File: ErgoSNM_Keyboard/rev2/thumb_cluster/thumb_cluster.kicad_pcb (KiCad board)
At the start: 2 copper layers, 57 x 38.2 mm, 19 parts, among them J1 Conn_01x08

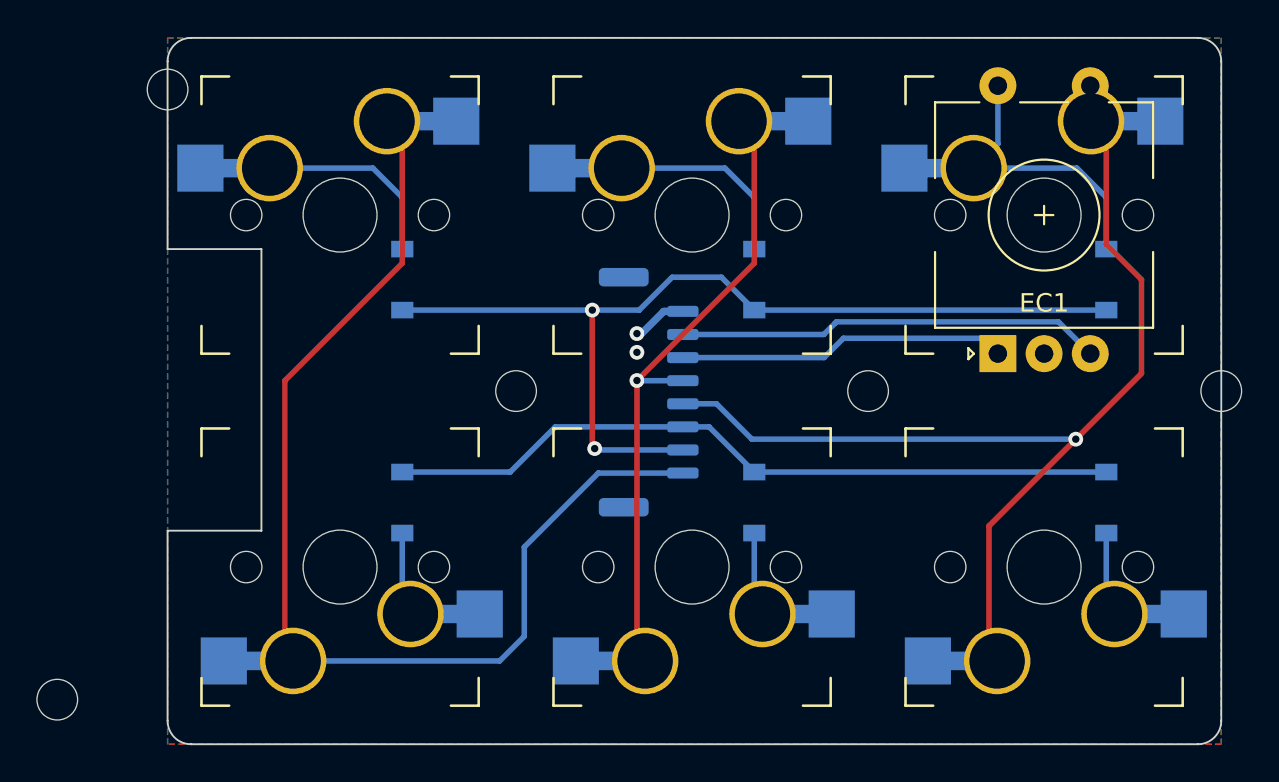
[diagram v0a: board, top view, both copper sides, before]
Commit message: Replace JST GH 1.25 connector with 0.5mm FPC
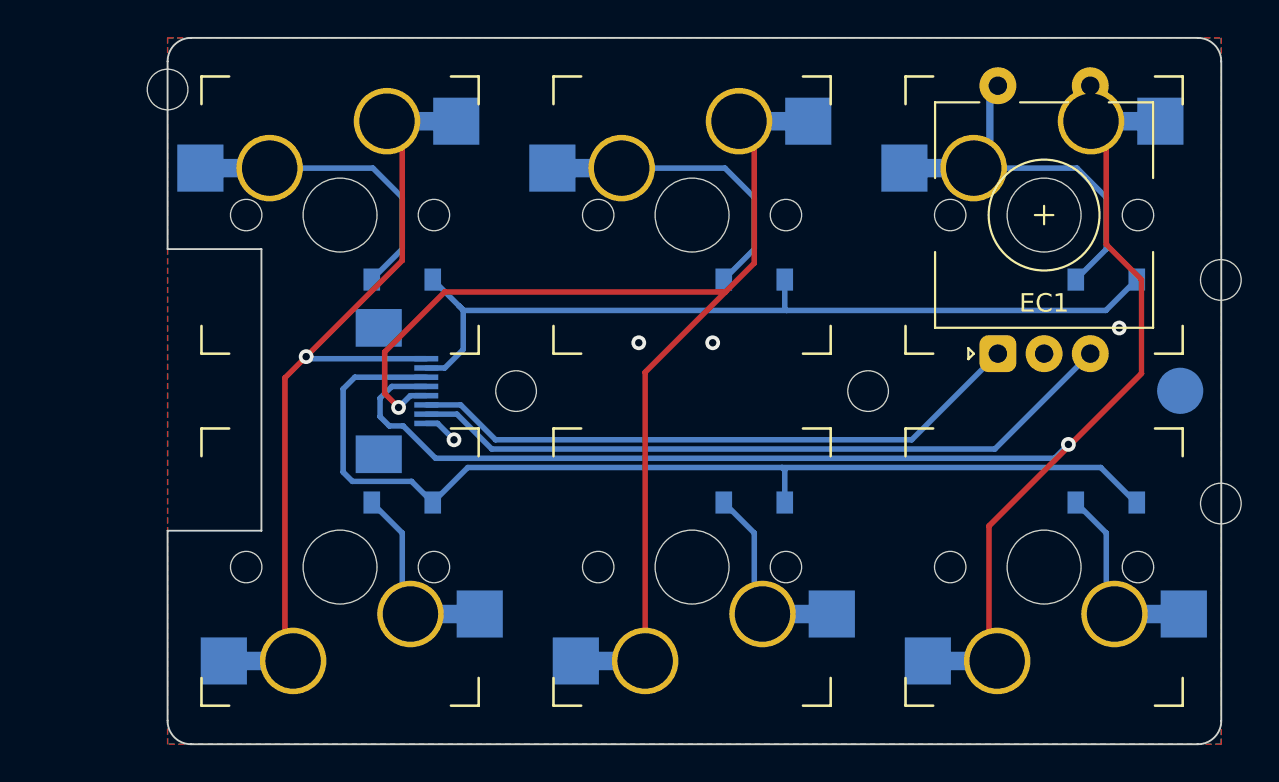
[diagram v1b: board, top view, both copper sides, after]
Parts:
- added TP1: TestPoint, TestPoint:TestPoint_Pad_D2.5mm, B.Cu at (116.9, 80.9)
- J1: footprint Connector_JST:JST_GH_SM08B-GHS-TB_1x08-1MP_P1.25mm_Horizontal -> ErgoSNM_Keyboard:FPC_8P_0.5mm_AFC01-S08FCA-00
- moved H3 63.9 mm to (119.1, 87.0)
- moved J1 15.0 mm to (73.1, 81.0), turned to -90 degrees
- moved H5 6.01 mm to (119.1, 74.9)
- turned D1 to 180 degrees
- turned D2 to 180 degrees
- turned D3 to 180 degrees
- turned D4 to 180 degrees
- turned D5 to 180 degrees
- turned D6 to 180 degrees
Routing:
- net COL_6: track 34.9 -> 57.5 mm
- net COL_5: track 60.5 -> 38.9 mm, vias 0 -> 1
- net COL_7: track 56.0 -> 76.3 mm
- net ROW_5: track 40.1 -> 56.4 mm
- net Encoder_A: track 17.8 -> 33.6 mm
- net Encoder_B: track 23.0 -> 38.9 mm
- net ROW_4: track 51.9 -> 46.1 mm, vias 2 -> 0
- net Net-(D3-Pad2): track 15.6 -> 18.0 mm
- net Net-(D2-Pad2): track 10.6 -> 13.0 mm
- net Net-(D1-Pad2): track 10.6 -> 13.0 mm
- net Net-(D6-Pad2): track 4.57 -> 6.90 mm
- net Net-(D5-Pad2): track 4.57 -> 6.90 mm
- net Net-(D4-Pad2): track 4.57 -> 6.90 mm
- net GND: track 2.98 -> 1.87 mm, vias 2 -> 4
